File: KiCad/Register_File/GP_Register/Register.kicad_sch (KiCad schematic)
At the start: 59 parts, among them J1 Conn_01x02_Pin, J2 Conn_01x02_Pin, J3 Conn_01x02_Pin, J4 Conn_01x08_Pin, J5 Conn_01x08_Pin, J6 Conn_01x04_Pin, J7 Conn_01x04_Pin, J8 Conn_01x04_Pin, J9 Conn_01x04_Pin, SW1 SW_SPDT, U1 74LS173, U2 74LS173, U3 74LS245, U4 74LS173, U5 74LS173, U6 74LS245

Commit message: finished registier file boards
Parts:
- removed SW1: SW_SPDT, Button_Switch_THT:SW_Slide_SPDT_Angled_CK_OS102011MA1Q, symbol Switch:SW_SPDT
- added C8, C9: 10n, Capacitor_THT:C_Disc_D3.8mm_W2.6mm_P2.50mm, symbol Device:C
- added SW2: SW_SPDT, Button_Switch_THT:SW_Slide_SPDT_Angled_CK_OS102011MA1Q, symbol Switch:SW_SPDT
- added U7, U8: 74LS245, Package_DIP:DIP-20_W7.62mm_Socket_LongPads, symbol 74xx:74LS245
- R10, R12, R13, R14, R15, R16, R17, R18, R2, R3, R4, R5, R6, R7, R8, R9: footprint Resistor_THT:R_Axial_DIN0204_L3.6mm_D1.6mm_P7.62mm_Horizontal -> Resistor_SMD:R_1206_3216Metric_Pad1.30x1.75mm_HandSolder
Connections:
- net +5V: now also C8.1, C9.1, SW2.3 (C), U7.1 (A->B), U7.20 (VCC), U8.1 (A->B), U8.20 (VCC)
- net GND: now also D1.1 (K), D10.1 (K), D11.1 (K), D12.1 (K), D13.1 (K), D14.1 (K), D15.1 (K), D16.1 (K), D2.1 (K), D3.1 (K), D4.1 (K), D5.1 (K), D6.1 (K), D7.1 (K), D8.1 (K), D9.1 (K), C8.2, C9.2, SW2.1 (A), U7.10 (GND), U8.10 (GND)
- net Y0: now also U7.2 (A0); no longer R2.1
- net Y1: now also U7.3 (A1); no longer R3.1
- net Y10: now also U8.4 (A2); no longer R13.1
- net Y11: now also U8.5 (A3); no longer R14.1
- net Y12: now also U8.6 (A4); no longer R15.1
- net Y13: now also U8.7 (A5); no longer R16.1
- net Y14: now also U8.8 (A6); no longer R17.1
- net Y15: now also U8.9 (A7); no longer R18.1
- net Y2: now also U7.4 (A2); no longer R4.1
- net Y3: now also U7.5 (A3); no longer R5.1
- net Y4: now also U7.6 (A4); no longer R6.1
- net Y5: now also U7.7 (A5); no longer R7.1
- net Y6: now also U7.8 (A6); no longer R8.1
- net Y7: now also U7.9 (A7); no longer R9.1
- net Y8: now also U8.2 (A0); no longer R10.1
- net Y9: now also U8.3 (A1); no longer R12.1
- net DE_B renamed ~{DE}
- net OE_B renamed ~{OE}
- new net: SW2.2 (B), U7.19 (CE), U8.19 (CE)
- new net LED_0: R2.1, U7.18 (B0)
- new net LED_1: R3.1, U7.17 (B1)
- new net LED_10: R13.1, U8.16 (B2)
- new net LED_11: R14.1, U8.15 (B3)
- new net LED_12: R15.1, U8.14 (B4)
- new net LED_13: R16.1, U8.13 (B5)
- new net LED_14: R17.1, U8.12 (B6)
- new net LED_15: R18.1, U8.11 (B7)
- new net LED_2: R4.1, U7.16 (B2)
- new net LED_3: R5.1, U7.15 (B3)
- new net LED_4: R6.1, U7.14 (B4)
- new net LED_5: R7.1, U7.13 (B5)
- new net LED_6: R8.1, U7.12 (B6)
- new net LED_7: R9.1, U7.11 (B7)
- new net LED_8: R10.1, U8.18 (B0)
- new net LED_9: R12.1, U8.17 (B1)
- no-connect marks 1 -> 0
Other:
- moved on the sheet: R10, R12, R13, R14, R15, R16, R17, R18, R2, R3, R4, R5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

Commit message: added more boards, added pcb standarts
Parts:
- added J10: Conn_01x02_Pin, elad_jst:JST_XH_S2B-XH-A-1_1x02_P2.50mm_Horizontal_fixed, symbol Connector:Conn_01x02_Pin
- C1, C2, C3, C4, C5, C7, C8, C9: footprint Capacitor_THT:C_Disc_D3.8mm_W2.6mm_P2.50mm -> Capacitor_SMD:C_1206_3216Metric_Pad1.33x1.80mm_HandSolder
- J1, J2, J3: footprint Connector_JST:JST_XH_S2B-XH-A_1x02_P2.50mm_Horizontal -> elad_jst:JST_XH_S2B-XH-A-1_1x02_P2.50mm_Horizontal_fixed
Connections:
- net +5V: now also J10.1 (Pin_1)
- net GND: now also J10.2 (Pin_2)
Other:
- note added: "Connectors"
- note removed: "CTRL connectors"
- moved on the sheet: J2, J3

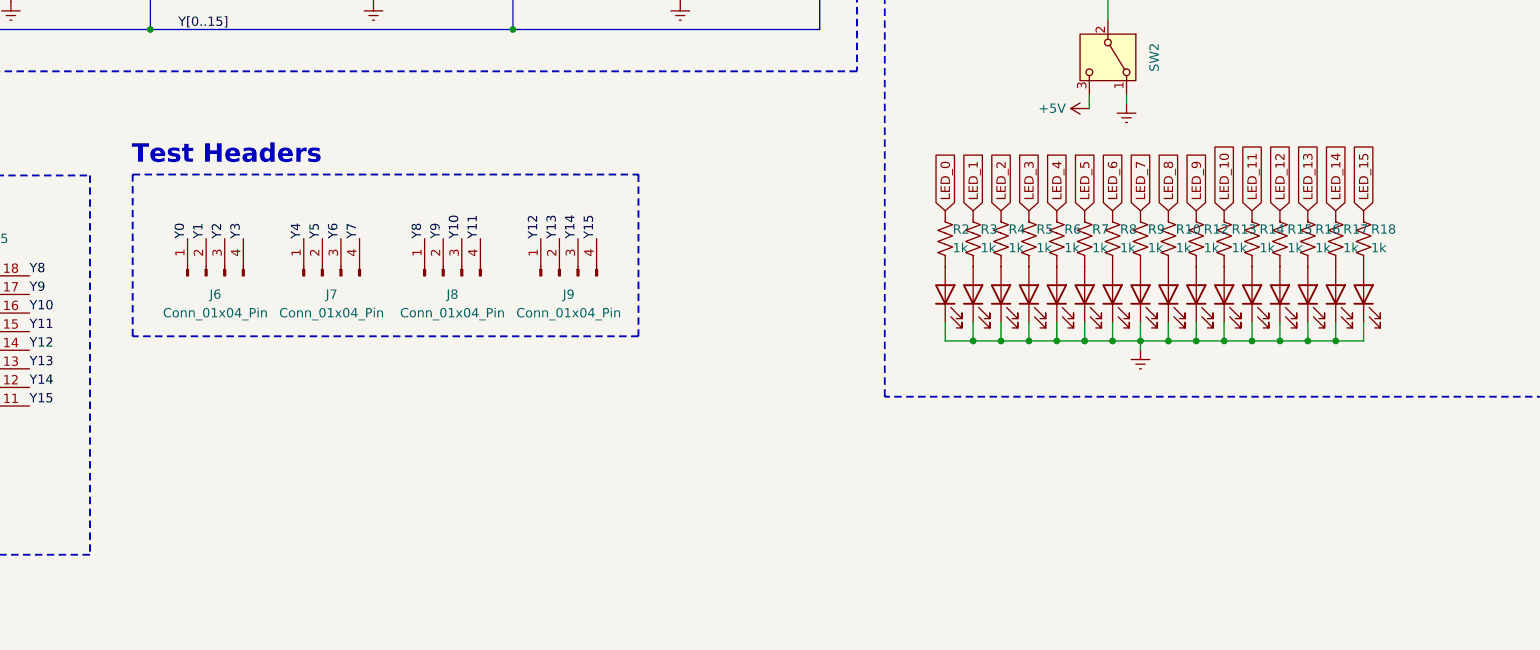
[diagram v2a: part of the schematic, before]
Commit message: created standarts for PCB's
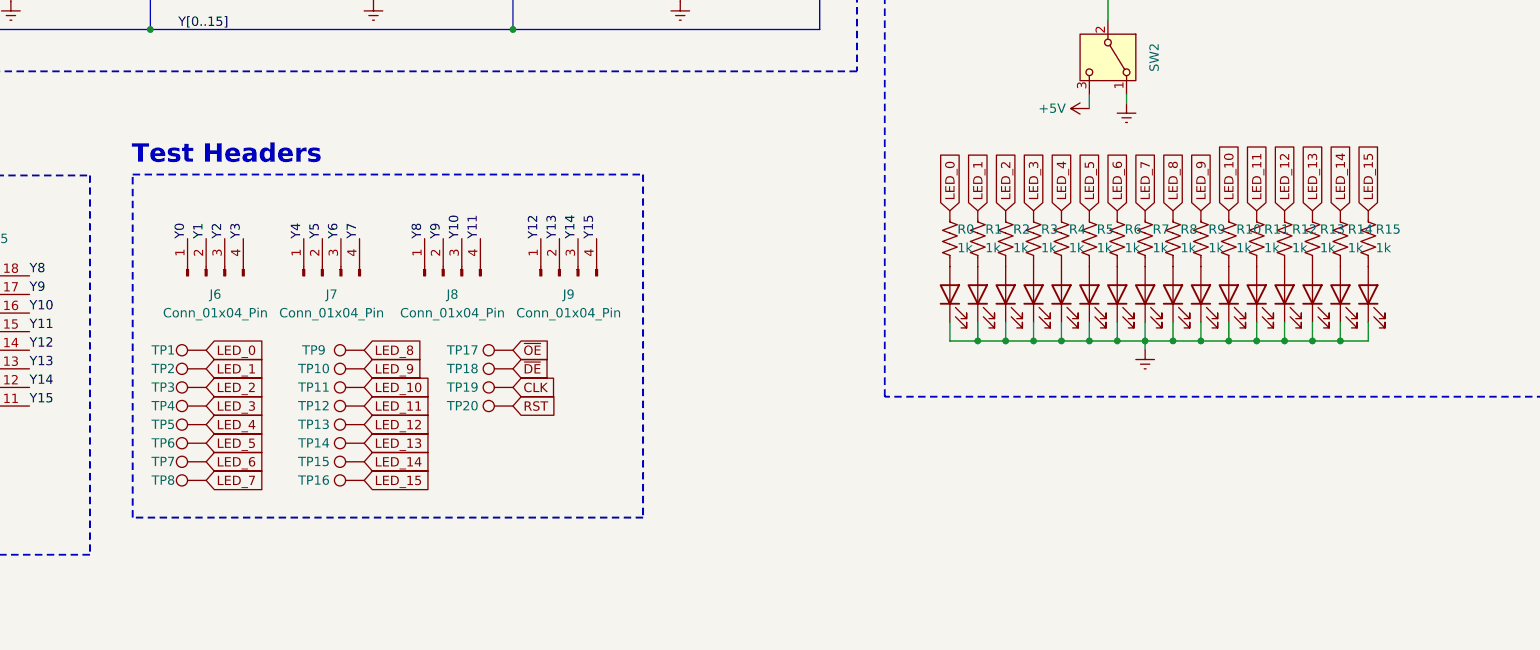
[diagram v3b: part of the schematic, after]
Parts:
- removed D16: LED, LED_THT:LED_Rectangular_W3.0mm_H2.0mm, symbol Device:LED
- removed R16, R17, R18: 1k, Resistor_SMD:R_1206_3216Metric_Pad1.30x1.75mm_HandSolder, symbol Device:R_US
- added D0: LED, LED_THT:LED_Rectangular_W3.0mm_H2.0mm, symbol Device:LED
- added R0, R1, R11: 1k, Resistor_SMD:R_1206_3216Metric_Pad1.30x1.75mm_HandSolder, symbol Device:R_US
- added TP1, TP10, TP11, TP12, TP13, TP14, TP15, TP16, TP17, TP18, TP19, TP2, TP20, TP3, TP4, TP5, TP6, TP7, TP8, TP9: TestPoint, TestPoint:TestPoint_Pad_D1.0mm, symbol Connector:TestPoint
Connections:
- net CLK: now also TP19.1
- net GND: now also D0.1 (K)
- net LED_0: now also R0.1, TP1.1; no longer R2.1
- net LED_1: now also R1.1, TP2.1; no longer R3.1
- net LED_10: now also R10.1, TP11.1; no longer R13.1
- net LED_11: now also R11.1, TP12.1; no longer R14.1
- net LED_12: now also R12.1, TP13.1; no longer R15.1
- net LED_13: now also R13.1, TP14.1
- net LED_14: now also R14.1, TP15.1
- net LED_15: now also R15.1, TP16.1
- net LED_2: now also R2.1, TP3.1; no longer R4.1
- net LED_3: now also R3.1, TP4.1; no longer R5.1
- net LED_4: now also R4.1, TP5.1; no longer R6.1
- net LED_5: now also R5.1, TP6.1; no longer R7.1
- net LED_6: now also R6.1, TP7.1; no longer R8.1
- net LED_7: now also R7.1, TP8.1; no longer R9.1
- net LED_8: now also R8.1, TP9.1; no longer R10.1
- net LED_9: now also R9.1, TP10.1; no longer R12.1
- net RST: now also TP20.1
- net ~{DE}: now also TP18.1
- net ~{OE}: now also TP17.1
- net at R13.2: now also D13.2 (A); no longer D11.2 (A)
- net at R12.2: now also D12.2 (A); no longer D10.2 (A)
- net at R6.2: now also D6.2 (A); no longer D5.2 (A)
- net at D9.2 (A): now also R9.2; no longer R10.2
- net at D3.2 (A): now also R3.2; no longer R4.2
- net at R15.2: now also D15.2 (A); no longer D13.2 (A)
- net at D7.2 (A): now also R7.2; no longer R8.2
- net at D4.2 (A): now also R4.2; no longer R5.2
- net at D2.2 (A): now also R2.2; no longer R3.2
- net at D8.2 (A): now also R8.2; no longer R9.2
- net at D1.2 (A): now also R1.2; no longer R2.2
- net at D14.2 (A): now also R14.2
- new net: D0.2 (A), R0.2
- new net: D10.2 (A), R10.2
- new net: D5.2 (A), R5.2
- new net: D11.2 (A), R11.2
